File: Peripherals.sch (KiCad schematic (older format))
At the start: 8 parts, among them U1 IMX6UL_BGA289

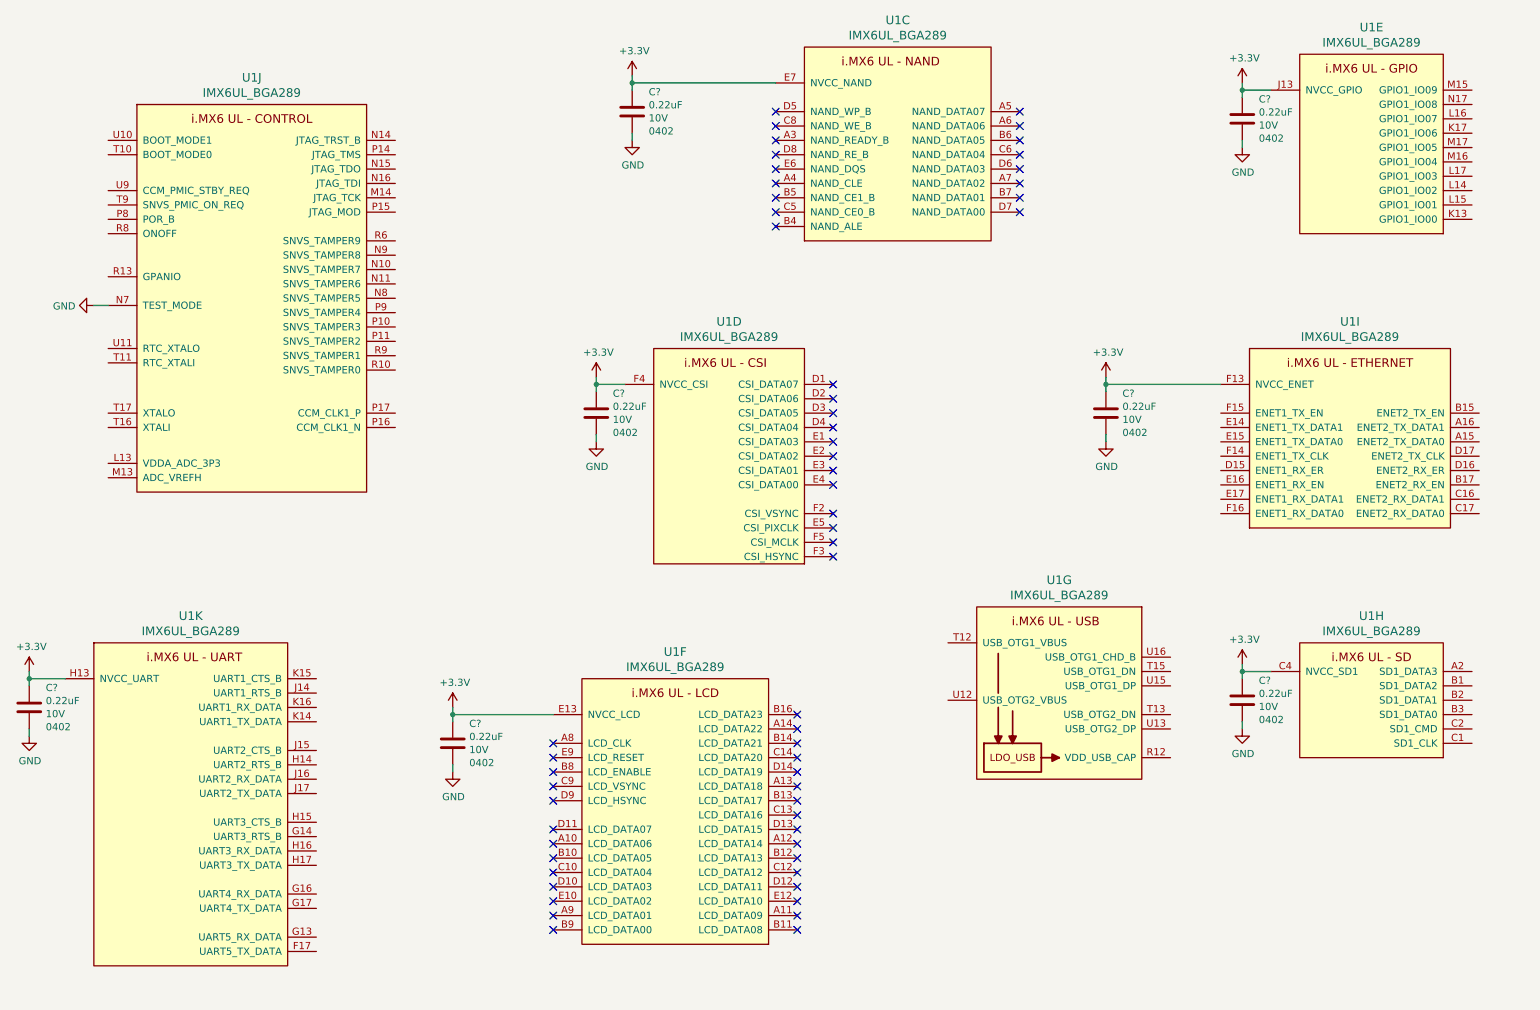
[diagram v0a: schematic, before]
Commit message: Added some LDO and connectors, still need to finish routing
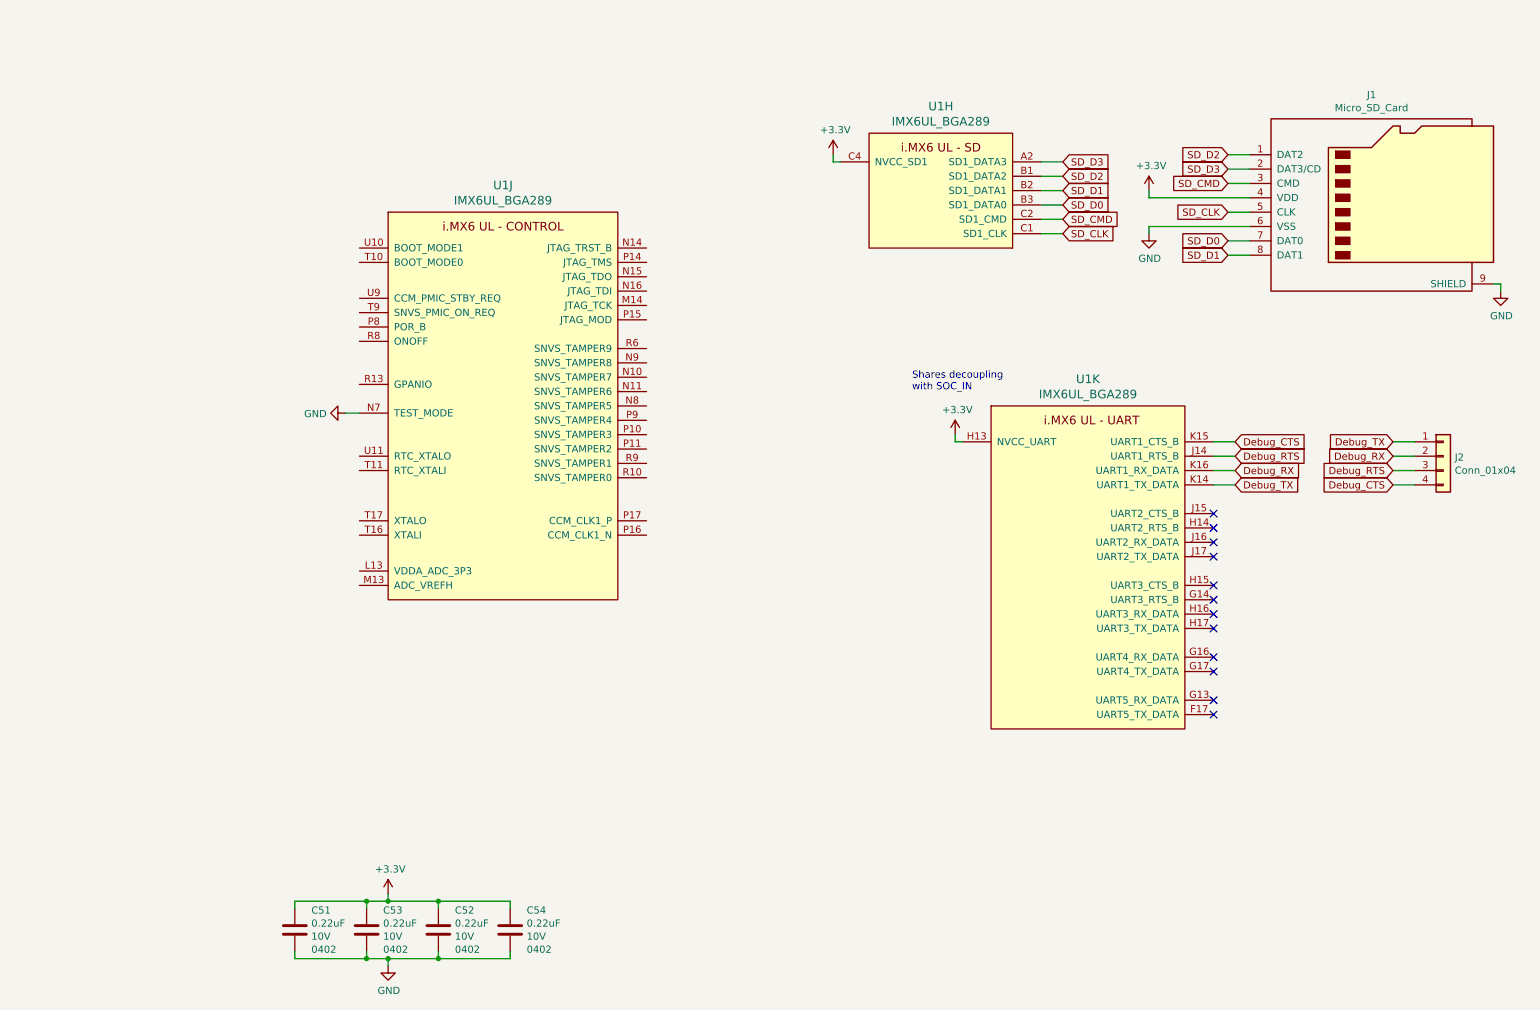
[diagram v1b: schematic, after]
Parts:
- removed C? (x3): 0.22uF, Capacitor_SMD:C_0402_1005Metric, symbol Device:C
- removed unit 3 of U1
- removed unit 4 of U1
- removed unit 5 of U1
- removed unit 6 of U1
- removed unit 7 of U1
- removed unit 9 of U1
- added J1: Micro_SD_Card, Connector_Card:microSD_HC_Molex_104031-0811, symbol Connector:Micro_SD_Card
- added J2: Conn_01x04, Connector_PinHeader_2.54mm:PinHeader_1x04_P2.54mm_Vertical, symbol Connector_Generic:Conn_01x04
- gave numbers to parts that had none: 4
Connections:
- net +3V3: now also J1.4 (VDD)
- net GND: now also J1.6 (VSS), J1.9 (SHIELD)
- net SD_D3: now reaches U1.A2 (SD1_DATA3)
- net SD_D3: now also J1.2 (DAT3/CD)
- net SD_D2: now reaches U1.B1 (SD1_DATA2)
- net SD_D2: now also J1.1 (DAT2)
- net SD_D1: now reaches U1.B2 (SD1_DATA1)
- net SD_D1: now also J1.8 (DAT1)
- net SD_D0: now reaches U1.B3 (SD1_DATA0)
- net SD_D0: now also J1.7 (DAT0)
- net SD_CLK: now reaches U1.C1 (SD1_CLK)
- net SD_CLK: now also J1.5 (CLK)
- net SD_CMD: now reaches U1.C2 (SD1_CMD)
- net SD_CMD: now also J1.3 (CMD)
- net Debug_RTS: now reaches U1.J14 (UART1_RTS_B)
- net Debug_RTS: now also J2.3 (Pin_3)
- net Debug_TX: now reaches U1.K14 (UART1_TX_DATA)
- net Debug_TX: now also J2.1 (Pin_1)
- net Debug_CTS: now reaches U1.K15 (UART1_CTS_B)
- net Debug_CTS: now also J2.4 (Pin_4)
- net Debug_RX: now reaches U1.K16 (UART1_RX_DATA)
- net Debug_RX: now also J2.2 (Pin_2)
- no-connect marks 58 -> 12
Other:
- note added: "Shares decoupling \nwith SOC_IN\n"
- moved on the sheet: C51, C52, C53, C54, U1H, U1J, U1K

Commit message: Finished first version of board
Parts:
- added C30, C32: 18pF, Capacitor_SMD:C_0402_1005Metric, symbol Device:C
- added Y1: Crystal_GND24, Crystal:Crystal_SMD_3225-4Pin_3.2x2.5mm, symbol Device:Crystal_GND24
- C51, C52, C53, C54: LCSC (none) -> C16772
- U1: LCSC (none) -> C414042
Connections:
- net +3V3: now also U1.L13 (VDDA_ADC_3P3), U1.M13 (ADC_VREFH)
- net GND: now also U1.P15 (JTAG_MOD), C30.2, C32.2, Y1.2, Y1.4
- net at U1.T16 (XTALI): now also C32.1, Y1.1
- net at U1.T17 (XTALO): now also C30.1, Y1.3
- net Debug_CTS: no longer names the net of J2.4 (Pin_4)
- net Debug_CTS: now also U1.K14 (UART1_TX_DATA); no longer U1.K15 (UART1_CTS_B)
- net Debug_RTS: no longer names the net of U1.J14 (UART1_RTS_B)
- net Debug_RTS: now also J2.2 (Pin_2); no longer J2.3 (Pin_3)
- net Debug_RX: no longer names the net of U1.K16 (UART1_RX_DATA)
- net Debug_RX: now also J2.3 (Pin_3); no longer J2.2 (Pin_2)
- net Debug_TX: no longer names the net of J2.1 (Pin_1)
- net Debug_TX: now also U1.K15 (UART1_CTS_B); no longer U1.K14 (UART1_TX_DATA)
- no-connect marks 12 -> 38
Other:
- moved on the sheet: J1, J2, U1H, U1J, U1K
